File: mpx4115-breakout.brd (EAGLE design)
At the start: 29.2 x 10.5 mm, 10 parts, among them U1 ADT7420UCPZ-R2, U2 ADXL345

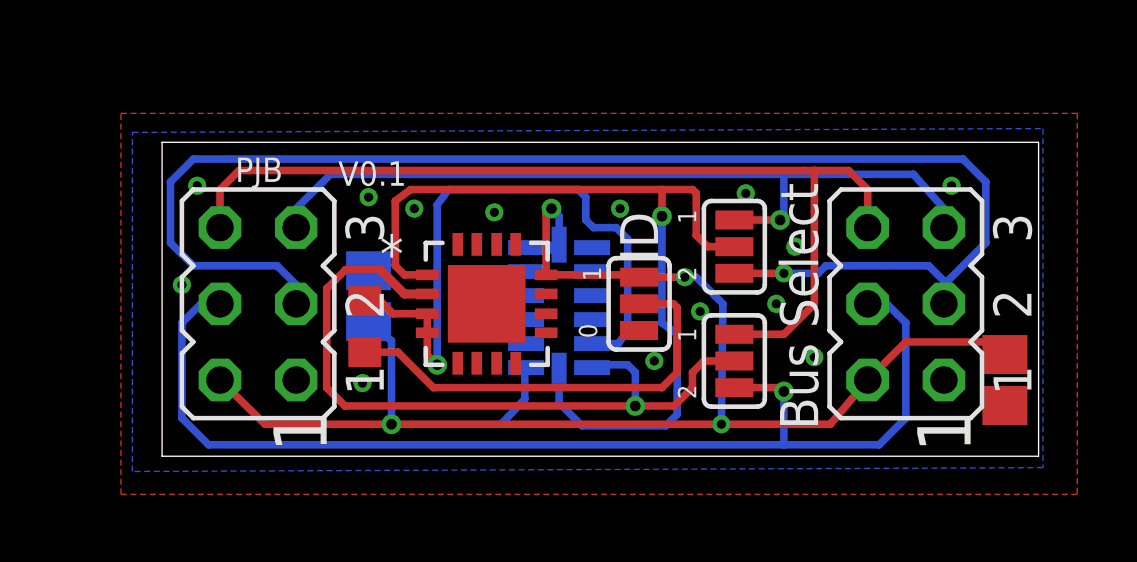
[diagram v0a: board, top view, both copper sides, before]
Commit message: breakout board for mpx4115 sensor with conditioning caps as reconmended in datasheet
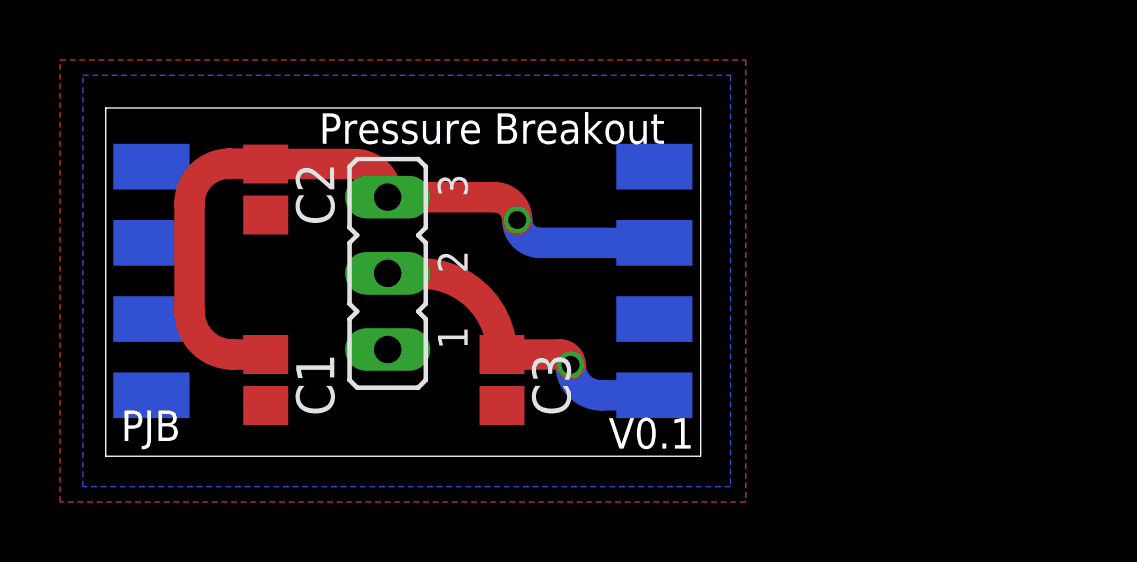
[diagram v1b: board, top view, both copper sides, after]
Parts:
- removed JP2, JP3: JUMPER-3SMD, SparkFun-Passives:SJ_3
- removed JP4, JP5: (no value), jumper:JP3Q
- removed R1: 10K, resistor:R0603
- removed U1: ADT7420UCPZ-R2, farnell-parts:QFN65P400X400X80-17N
- removed U2: ADXL345, SparkFun-Sensors:LGA14
- added C3: 470pF, resistor:C0805
- added U$1: MPX4115A, mountainsensing:MPX4115A
- C1: value (none) -> 1uF
- C2: value (none) -> 10nF
- JP1: value JUMPER-3SMD -> (none); device SparkFun-Passives:SJ_3 -> jumper:JP2
- moved C2 25.4 mm to (5.33, 8.89)
- moved JP1 8.44 mm to (9.40, 6.10)
- moved C1 4.42 mm to (5.33, 2.54), flipped to the top, turned to 270 degrees
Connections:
- removed net ADD: R1.2, U1.3, U1.4, U2.12
- removed net ADD_SEL: JP1.2, R1.1
- removed net SCL: JP3.2, U1.1, U2.14
- removed net SCL1: JP3.3, JP4.5, JP5.5
- removed net SCL2: JP3.1, JP4.3, JP5.3
- removed net SDA: JP2.2, U1.2, U2.13
- removed net SDA1: JP2.3, JP4.6, JP5.6
- removed net SDA2: JP2.1, JP4.4, JP5.4
- new net AOUT: C3.1, JP1.2, U$1.4
- net GND: now also C3.2, U$1.3; no longer JP4.1, JP5.1, U1.11, U2.2, U2.4, U2.5
- net VCC: now also U$1.2; no longer JP4.2, JP5.2, U1.12, U2.1, U2.6, U2.7
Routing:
- net SCL2: track 47.3 -> 0.00 mm, vias 1 -> 0
- net SDA2: track 37.8 -> 0.00 mm, vias 1 -> 0
- net SDA1: track 32.2 -> 0.00 mm
- net SCL: track 29.6 -> 0.00 mm, vias 1 -> 0
- net VCC: track 53.3 -> 23.9 mm, vias 4 -> 1
- net SCL1: track 26.9 -> 0.00 mm, vias 1 -> 0
- net SDA: track 24.7 -> 0.00 mm, vias 1 -> 0
- net ADD: track 21.6 -> 0.00 mm, vias 1 -> 0
- net ADD_SEL: track 14.6 -> 0.00 mm
- net AOUT: track 0.00 -> 10.6 mm, vias 0 -> 1
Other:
- board size 29.2 x 10.5 mm -> 19.8 x 11.6 mm
- board text added: "Pressure Breakout"
- board text removed: "0"
- board text removed: "1"
- board text removed: "2"
- board text removed: "Bus Select"
- board text removed: "ID"
